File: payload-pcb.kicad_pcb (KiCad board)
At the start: 4 copper layers, 127 x 76.2 mm, 112 parts, among them J1 POWER_IN, J10 GPIO0, J12 I2C, J13 GPIO1, J14 CAN, J15 CAN, J16 SCOOP1, J17 SCOOP2, J18 ACTUATOR, J19 DRILL, J2 POWER_OUT, J20 SERVO5, J21 SERVO6, J22 SERVO7, J23 SERVO8, J5 MOIST, J6 TEMP, J7 POT3, J9 RELAYS, Q1 SUD50P10-43L-GE3, Q2 SUD50P10-43L-GE3, Q3 SUD50P10-43L-GE3, Q4 DMG2305UX, Q5 Q_NMOS, Q6 Q_NMOS, Q7 Q_NMOS, Q8 Q_NMOS, U12 +3V3@2A, U14 Pico, U15 74HCT244, U22 MCP2562, U23 MCP2515, U8 PCA9555PWR, U9 +5V@2A, Y1 8MHz

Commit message: more cleanup and added notes for review
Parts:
- added R20: 1k, Resistor_SMD:R_0805_2012Metric_Pad1.20x1.40mm_HandSolder, F.Cu at (1.88, 0.97)
- added R21: 150, Resistor_SMD:R_0805_2012Metric_Pad1.20x1.40mm_HandSolder, F.Cu at (1.88, 3.92)
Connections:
- net GP21 renamed DIGITAL_GP21
- net GP22 renamed DIGITAL_GP22
- net INT renamed ~{CAN_INTERRUPT}
- net NEW_GP14 renamed DIGITAL_GP14
- net NEW_GP15 renamed DIGITAL_GP15
- J10 pad 1: Net-(J10-Pin_1) -> /GPIO/Payload_S1
- J10 pad 2: Net-(J10-Pin_2) -> /GPIO/Payload_S2
- J10 pad 3: Net-(J10-Pin_3) -> /GPIO/Payload_S3
- J10 pad 4: Net-(J10-Pin_4) -> /GPIO/Payload_S4
- J10 pad 5: /GPIO/Payload_S1 -> Net-(J10-Pin_5)
- J10 pad 6: /GPIO/Payload_S2 -> Net-(J10-Pin_6)
- J10 pad 7: /GPIO/Payload_S3 -> Net-(J10-Pin_7)
- J10 pad 8: /GPIO/Payload_S4 -> Net-(J10-Pin_8)
- U8 pad 10: /GPIO/Payload_S3 -> Net-(J10-Pin_7)
- U8 pad 11: /GPIO/Payload_S4 -> Net-(J10-Pin_8)
- U8 pad 4: Net-(J10-Pin_1) -> /GPIO/Payload_S1
- U8 pad 5: Net-(J10-Pin_2) -> /GPIO/Payload_S2
- U8 pad 6: Net-(J10-Pin_3) -> /GPIO/Payload_S3
- U8 pad 7: Net-(J10-Pin_4) -> /GPIO/Payload_S4
- U8 pad 8: /GPIO/Payload_S1 -> Net-(J10-Pin_5)
- U8 pad 9: /GPIO/Payload_S2 -> Net-(J10-Pin_6)
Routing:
- net (no net): vias 0 -> 102

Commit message: pcb review session notes
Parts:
- removed R20: 1k, Resistor_SMD:R_0805_2012Metric_Pad1.20x1.40mm_HandSolder
- removed R21: 150, Resistor_SMD:R_0805_2012Metric_Pad1.20x1.40mm_HandSolder
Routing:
- net Net-(J10-Pin_8): track 0.00 -> 8.38 mm
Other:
- board text added: "University Rover Challenge Payload PCB v5.0 by Austin Driggs 2025-2026"
- board text removed: "University Rover Challenge Payload PCB by Austin Driggs 2025-2026"

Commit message: major rework again after the meeting
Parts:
- removed C10: 22 uF, Payload_PCB_v3.1:UCM1H220MCL1GS
- removed C11, C12, C13: 0.1 uF, Capacitor_SMD:C_1206_3216Metric_Pad1.33x1.80mm_HandSolder
- removed D11: LED4, LED_SMD:LED_0805_2012Metric_Pad1.15x1.40mm_HandSolder
- removed D12: LED3, LED_SMD:LED_0805_2012Metric_Pad1.15x1.40mm_HandSolder
- removed D4: +40V, LED_SMD:LED_0805_2012Metric_Pad1.15x1.40mm_HandSolder
- removed D6: VDC, LED_SMD:LED_0805_2012Metric_Pad1.15x1.40mm_HandSolder
- removed D7: +5V, LED_SMD:LED_0805_2012Metric_Pad1.15x1.40mm_HandSolder
- removed D8: +3V3, LED_SMD:LED_0805_2012Metric_Pad1.15x1.40mm_HandSolder
- removed F2, F3: Fuse, Fuse:Fuseholder_Blade_Mini_Keystone_3568
- removed J10: GPIO0, Connector_Molex:Molex_PicoBlade_53047-0810_1x08_P1.25mm_Vertical
- removed J13: GPIO1, Connector_Molex:Molex_PicoBlade_53047-0810_1x08_P1.25mm_Vertical
- removed J20: SERVO5, Connector_Molex:Molex_PicoBlade_53047-0310_1x03_P1.25mm_Vertical
- removed J21: SERVO6, Connector_Molex:Molex_PicoBlade_53047-0310_1x03_P1.25mm_Vertical
- removed J22: SERVO7, Connector_Molex:Molex_PicoBlade_53047-0310_1x03_P1.25mm_Vertical
- removed J23: SERVO8, Connector_Molex:Molex_PicoBlade_53047-0310_1x03_P1.25mm_Vertical
- removed JP1, JP2, JP3, JP4: SolderJumper_2_Open, Jumper:SolderJumper-2_P1.3mm_Open_RoundedPad1.0x1.5mm
- removed Q3: SUD50P10-43L-GE3, Package_TO_SOT_SMD:TO-252-2
- removed Q7, Q8: Q_NMOS, Package_TO_SOT_SMD:TSOT-23
- removed R15: 1k, Resistor_SMD:R_0805_2012Metric_Pad1.20x1.40mm_HandSolder
- removed R16, R18: 150, Resistor_SMD:R_0805_2012Metric_Pad1.20x1.40mm_HandSolder
- removed R19: 62, Resistor_SMD:R_0805_2012Metric_Pad1.20x1.40mm_HandSolder
- removed TP14: LED4, TestPoint:TestPoint_Pad_D1.0mm
- removed TP16: LED3, TestPoint:TestPoint_Pad_D1.0mm
- removed TP2: +BATT_IN, TestPoint:TestPoint_Pad_D2.0mm
- removed TP3: +VDC_IN, TestPoint:TestPoint_Pad_D2.0mm
- removed TP4, TP6: +12V_IN, TestPoint:TestPoint_Pad_D2.0mm
- removed U15: 74HCT244, Package_SO:SO-20_12.8x7.5mm_P1.27mm
- removed U8: PCA9555PWR, Package_SO:TSSOP-24_4.4x7.8mm_P0.65mm
- added C8: 0.1 uF, Capacitor_SMD:C_1206_3216Metric_Pad1.33x1.80mm_HandSolder, F.Cu at (162.1, 69.3)
- added J3: UART, Connector_Molex:Molex_PicoBlade_53047-0410_1x04_P1.25mm_Vertical, F.Cu at (191.1, 68.1)
- added J4: USB, Connector_USB:USB_Micro-B_Wuerth_629105150521, F.Cu at (153.2, 69.2)
- added R10: 45m, Resistor_SMD:R_1206_3216Metric_Pad1.30x1.75mm_HandSolder, F.Cu at (121.8, 90.0)
- added R9: 45m, Resistor_SMD:R_1206_3216Metric_Pad1.30x1.75mm_HandSolder, F.Cu at (124.1, 90.0)
- added U1: SN74AHCT126DR, Package_SO:SOIC-14_3.9x8.7mm_P1.27mm, F.Cu at (139.6, 76.1)
- added U2: FT230XS, Package_SO:SSOP-20_3.9x8.7mm_P0.635mm, F.Cu at (166.8, 72.1)
- added U3: LTC2990, Package_SO:MSOP-10_3x3mm_P0.5mm, F.Cu at (132.1, 89.6)
- C1: value 0.1 uF -> 22 uF; footprint Capacitor_SMD:C_1206_3216Metric_Pad1.33x1.80mm_HandSolder -> Capacitor_THT:CP_Radial_D10.0mm_P5.00mm
- C20: footprint Payload_PCB_v3.1:UCM1H220MCL1GS -> Capacitor_SMD:C_Elec_4x5.4
- C4: value 0.1 uF -> 47p; footprint Capacitor_SMD:C_1206_3216Metric_Pad1.33x1.80mm_HandSolder -> Capacitor_SMD:C_0603_1608Metric_Pad1.08x0.95mm_HandSolder
- C5: value 22 uF -> 47p; footprint Payload_PCB_v3.1:UCM1H220MCL1GS -> Capacitor_SMD:C_0603_1608Metric_Pad1.08x0.95mm_HandSolder
- C9: value 0.1 uF -> 470p; footprint Capacitor_SMD:C_1206_3216Metric_Pad1.33x1.80mm_HandSolder -> Capacitor_SMD:C_0603_1608Metric_Pad1.08x0.95mm_HandSolder
- D10: value LED2 -> BAD
- D2, D3: value BZT52C10-TP -> +12V; footprint Diode_SMD:D_SOD-123 -> LED_SMD:LED_0805_2012Metric_Pad1.15x1.40mm_HandSolder
- D9: value LED1 -> GOOD
- F1: footprint Fuse:Fuseholder_Blade_Mini_Keystone_3568 -> Fuse:Fuse_1210_3225Metric
- J1: footprint Connector_Molex:Molex_Mini-Fit_Jr_5569-06A2_2x03_P4.20mm_Horizontal -> Connector_Molex:Molex_Micro-Fit_3.0_43045-0200_2x01_P3.00mm_Horizontal
- J16: value SCOOP1 -> SCOOP
- J17: value SCOOP2 -> MANIPULATOR
- J18: value ACTUATOR -> SERVO3
- J19: value DRILL -> SERVO4
- J2: footprint Connector_Molex:Molex_Mini-Fit_Jr_5569-12A2_2x06_P4.20mm_Horizontal -> Connector_Molex:Molex_Micro-Fit_3.0_43045-0600_2x03_P3.00mm_Horizontal
- J7: value POT3 -> MANIPULATOR
- J9: value RELAYS -> GPIO
- Q2: value SUD50P10-43L-GE3 -> MMBT3904; footprint Package_TO_SOT_SMD:TO-252-2 -> Package_TO_SOT_SMD:SOT-23
- R17: footprint Resistor_SMD:R_0805_2012Metric_Pad1.20x1.40mm_HandSolder -> Resistor_SMD:R_0603_1608Metric_Pad0.98x0.95mm_HandSolder
- R3, R4: value 100k -> 511; footprint Resistor_SMD:R_0805_2012Metric_Pad1.20x1.40mm_HandSolder -> Resistor_SMD:R_0603_1608Metric_Pad0.98x0.95mm_HandSolder
- R6: value 511 -> 27; footprint Resistor_SMD:R_0805_2012Metric_Pad1.20x1.40mm_HandSolder -> Resistor_SMD:R_0603_1608Metric_Pad0.98x0.95mm_HandSolder
- R7: value 10k -> 27; footprint Resistor_SMD:R_0805_2012Metric_Pad1.20x1.40mm_HandSolder -> Resistor_SMD:R_0603_1608Metric_Pad0.98x0.95mm_HandSolder
- R8: value 511 -> 45m; footprint Resistor_SMD:R_0805_2012Metric_Pad1.20x1.40mm_HandSolder -> Resistor_SMD:R_1206_3216Metric_Pad1.30x1.75mm_HandSolder
- TP11: moved to B.Cu
- U14: value Pico -> PI_PICO
- moved C3 57.8 mm to (171.4, 72.6), turned to -90 degrees
- moved G*** 56.5 mm to (175.4, 89.4)
- moved TP10 53.9 mm to (111.8, 123.3), turned to 90 degrees
- moved R4 51.4 mm to (103.8, 102.1), turned to -90 degrees
- moved C1 48.6 mm to (120.9, 74.2), turned to 0 degrees
- moved R3 45.6 mm to (105.4, 102.1), turned to -90 degrees
- moved C4 43.8 mm to (154.9, 73.3), turned to 180 degrees
- moved C5 39.5 mm to (151.6, 73.3)
- moved TP9 39.4 mm to (126.7, 82.5), turned to -90 degrees
- moved R7 38.7 mm to (152.5, 75.7), turned to -90 degrees
- moved D3 37.8 mm to (115.2, 105.5), turned to 180 degrees
- moved R8 35.5 mm to (126.4, 90.0), turned to 90 degrees
- moved D2 34.3 mm to (115.2, 103.4), turned to 180 degrees
- moved C9 33.9 mm to (132.1, 93.6), turned to 180 degrees
- moved J15 33.6 mm to (165.6, 111.6), turned to 180 degrees
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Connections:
- net ANALOG_POT3 renamed ANALOG_MANIPULATOR
- net DIGITAL_GP14 renamed DIGITAL_LIMIT_SW1
- net DIGITAL_GP15 renamed DIGITAL_LIMIT_SW2
- net DIGITAL_GP21 renamed DIGITAL_RELAY1
- net DIGITAL_GP22 renamed DIGITAL_RELAY2
- net LED1 renamed /Pi Pico/LED_GOOD
- net LED2 renamed /Pi Pico/LED_BAD
- C1 pad 1: GND -> +12V
- C1 pad 2: +12V -> GND
- C2 pad 2: +3.3V -> +5V
- C25 pad 1: VDC -> +5V
- C3 pad 2: +BATT -> +5V
- C4 pad 2: +12V -> /USB/USB-
- C5 pad 1: +12V -> GND
- C5 pad 2: GND -> /USB/USB+
- C9 pad 1: GND -> Net-(Q2-E)
- C9 pad 2: +BATT -> Net-(Q2-B)
- D1 pad 1: +12V -> /Power/+12V_PROTECTED
- D10 pad 1: GND -> Net-(D10-K)
- D2 pad 1: +BATT -> GND
- D3 pad 1: Net-(D3-K) -> GND
- D9 pad 1: GND -> Net-(D9-K)
- J1 pad 2: GND -> /Power/+12V_IN
- J12 pad 2: I2C0_SCL -> I2C0_SDA
- J12 pad 3: I2C0_SDA -> I2C0_SCL
- J16 pad 1: VDC -> +5V
- J17 pad 1: VDC -> +5V
- J18 pad 1: VDC -> +5V
- J19 pad 1: VDC -> +5V
- J2 pad 4: GND -> +12V
- J2 pad 5: GND -> +5V
- J2 pad 6: GND -> +3.3V
- Q1 pad 3: +12V -> /Power/+12V_PROTECTED
- Q2 pad 1: Net-(D2-A) -> Net-(Q2-B)
- Q2 pad 2: Net-(Q2-D) -> Net-(Q2-E)
- Q2 pad 3: +BATT -> Net-(Q2-B)
- Q4 pad 3: +3.3V -> +5V
- Q5 pad 1: Net-(Q5-D) -> Net-(D9-K)
- Q5 pad 3: Net-(D9-A) -> GND
- Q6 pad 1: Net-(Q6-D) -> Net-(D10-K)
- Q6 pad 3: Net-(D10-A) -> GND
- R1 pad 1: Net-(Q5-D) -> Net-(D9-A)
- R3 pad 2: GND -> +5V
- R4 pad 2: GND -> +3.3V
- R5 pad 1: Net-(Q6-D) -> Net-(D10-A)
- R6 pad 1: Net-(Q7-D) -> /USB/USB-
- R6 pad 2: +3.3V -> Net-(U2-USBDM)
- R7 pad 1: Net-(U8-~{INT}) -> /USB/USB+
- R7 pad 2: +3.3V -> Net-(U2-USBDP)
- R8 pad 1: Net-(Q8-D) -> /Power/+12V_PROTECTED
- R8 pad 2: +3.3V -> +12V
- U14 pad 10: SERVO6_PICO -> unconnected-(U14-GPIO7-Pad10)
- U14 pad 11: SERVO7_PICO -> /Pi Pico/UART1_TX
- U14 pad 12: SERVO8_PICO -> /Pi Pico/UART1_RX
- U14 pad 16: LED3 -> UART0_TX
- U14 pad 17: LED4 -> UART0_RX
- U14 pad 9: SERVO5_PICO -> unconnected-(U14-GPIO6-Pad9)
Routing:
- net Net-(J10-Pin_8): track 8.38 -> 0.00 mm
- net (no net): vias 102 -> 0
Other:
- board size 127 x 76.2 mm -> 101.6 x 63.5 mm

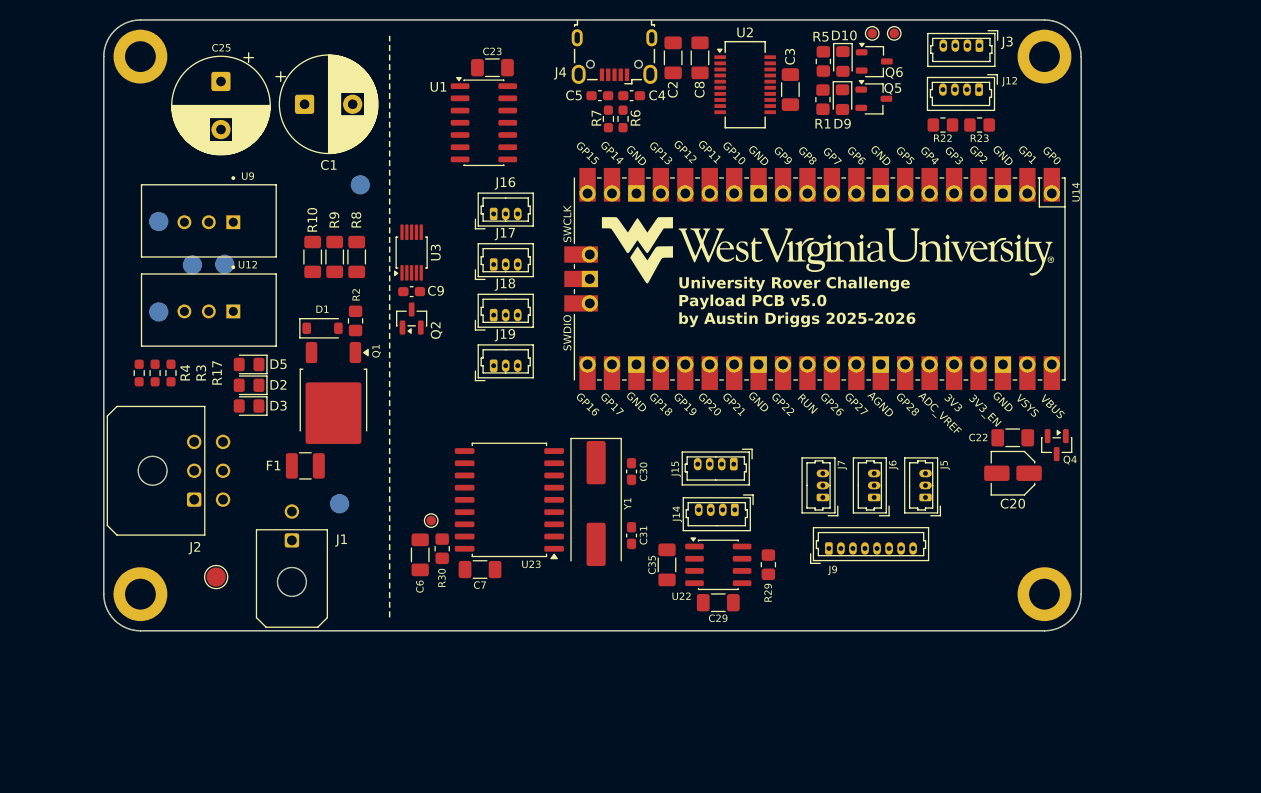
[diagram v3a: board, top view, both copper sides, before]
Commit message: major finishing touches:     - major rework for v5.1     - silkscreen and stuff     - impednace for USB and CAN lines     - schematic comments     - symbol, footprint, and model library updates
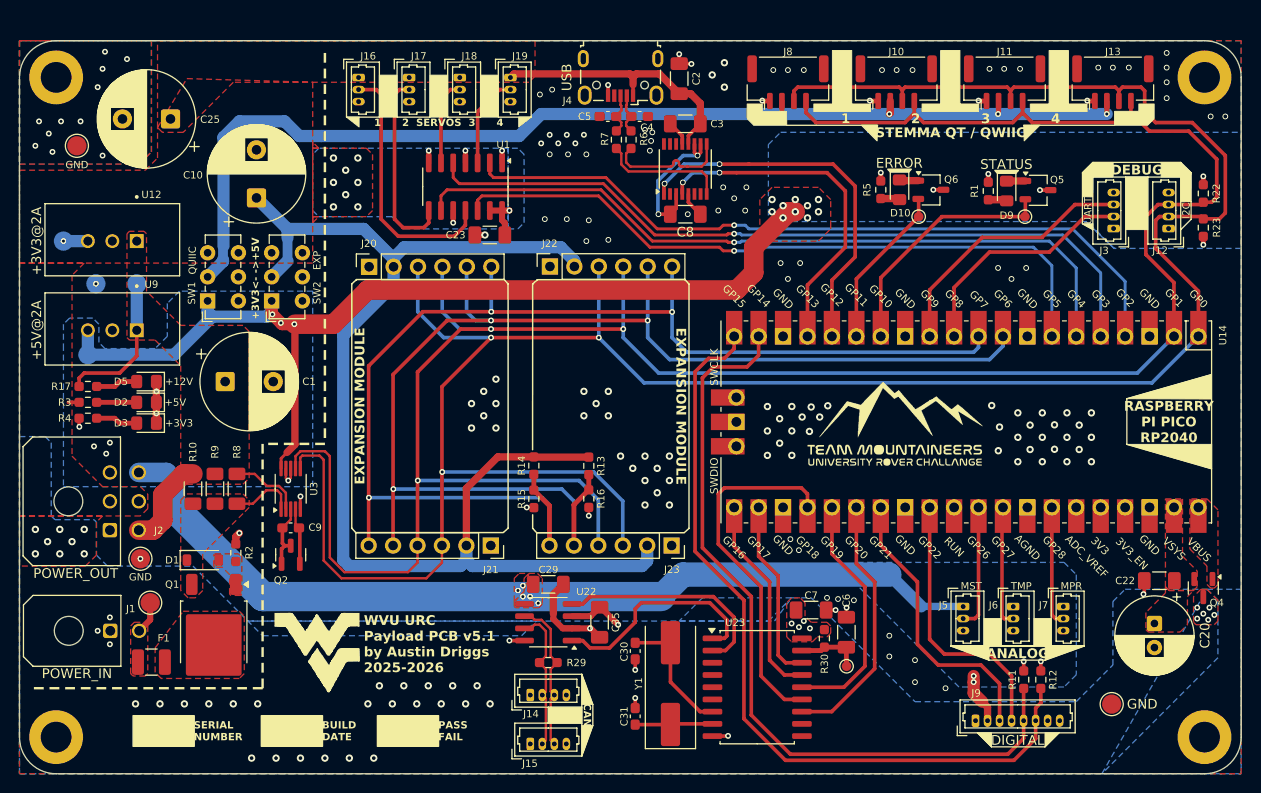
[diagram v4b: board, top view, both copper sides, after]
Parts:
- removed G***: LOGO, Payload_PCB_v3.1:Flying_WV_Logo_Large
- added C10: 1000uF, Capacitor_THT:CP_Radial_D10.0mm_P5.00mm, F.Cu at (116.0, 83.9)
- added J10: QWIIC3, Connector_JST:JST_GH_BM04B-GHS-TBT_1x04-1MP_P1.25mm_Vertical, F.Cu at (182.5, 71.9)
- added J11: QWIIC2, Connector_JST:JST_GH_BM04B-GHS-TBT_1x04-1MP_P1.25mm_Vertical, F.Cu at (193.7, 71.9)
- added J13: QWIIC1, Connector_JST:JST_GH_BM04B-GHS-TBT_1x04-1MP_P1.25mm_Vertical, F.Cu at (205.0, 71.9)
- added J20: EXP1, Connector_PinSocket_2.54mm:PinSocket_1x06_P2.54mm_Vertical, F.Cu at (127.7, 91.1)
- added J21: EXP2, Connector_PinSocket_2.54mm:PinSocket_1x06_P2.54mm_Vertical, F.Cu at (140.3, 120.0)
- added J22: EXP3, Connector_PinSocket_2.54mm:PinSocket_1x06_P2.54mm_Vertical, F.Cu at (146.5, 91.0)
- added J23: EXP4, Connector_PinSocket_2.54mm:PinSocket_1x06_P2.54mm_Vertical, F.Cu at (159.1, 120.0)
- added J8: QWIIC4, Connector_JST:JST_GH_BM04B-GHS-TBT_1x04-1MP_P1.25mm_Vertical, F.Cu at (171.2, 71.9)
- added R11: 10k, Resistor_SMD:R_0603_1608Metric_Pad0.98x0.95mm_HandSolder, F.Cu at (195.7, 134.0)
- added R12: 10k, Resistor_SMD:R_0603_1608Metric_Pad0.98x0.95mm_HandSolder, F.Cu at (197.5, 134.0)
- added R13: 10k, Resistor_SMD:R_0603_1608Metric_Pad0.98x0.95mm_HandSolder, F.Cu at (150.5, 111.8)
- added R14: 10k, Resistor_SMD:R_0603_1608Metric_Pad0.98x0.95mm_HandSolder, F.Cu at (144.8, 111.7)
- added R15: 10k, Resistor_SMD:R_0603_1608Metric_Pad0.98x0.95mm_HandSolder, F.Cu at (144.8, 115.2)
- added R16: 10k, Resistor_SMD:R_0603_1608Metric_Pad0.98x0.95mm_HandSolder, F.Cu at (150.5, 115.2)
- added SW1: QUIIC, Button_Switch_THT:SW_E-Switch_EG1271_SPDT, F.Cu at (110.9, 94.6)
- added SW2: EXP, Button_Switch_THT:SW_E-Switch_EG1271_SPDT, F.Cu at (117.5, 94.6)
- added TP2: GND, TestPoint:TestPoint_Pad_D2.0mm, F.Cu at (204.9, 136.5)
- C1: value 22 uF -> 1000uF
- C2, C22, C23, C29, C3, C35, C6, C7, C8: value 0.1 uF -> 0.1uF
- C20: value 10 uF -> 10uF; footprint Capacitor_SMD:C_Elec_4x5.4 -> Capacitor_THT:CP_Radial_D8.0mm_P2.50mm
- C25: value 100 uF -> 1000uF
- C30, C31: value 22 pF -> 22pF
- D10: value BAD -> ERROR
- D2: value +12V -> +5V
- D3: value +12V -> +3V3
- D9: value GOOD -> STATUS
- F1: value Fuse -> PTC
- J5: value MOIST -> MST
- J6: value TEMP -> TMP
- J7: value MANIPULATOR -> MPR
- J9: value GPIO -> DIGITAL
- Q5, Q6: value Q_NMOS -> 2N7002
- R1, R2, R22, R23, R29, R30, R5: footprint Resistor_SMD:R_0805_2012Metric_Pad1.20x1.40mm_HandSolder -> Resistor_SMD:R_0603_1608Metric_Pad0.98x0.95mm_HandSolder
- R10, R8, R9: value 45m -> 30m
- R6, R7: value 27 -> 22
- TP1: moved to F.Cu
- TP10, TP11: value +12V_IN -> GND
- TP5: value +12V_IN -> +12V
- TP7: value +12V_IN -> +5V
- TP8: value +12V_IN -> +3V3
- TP9: value +12V_IN -> GND; moved to F.Cu
- U12, U9: footprint Payload_PCB_v3.1:CONV_TSR_2-2433 -> footprints:TSR_2-24xx
- U14: footprint MCU_RaspberryPi_and_Boards:RPi_Pico_SMD_TH -> footprints:RPi_Pico_SMD_TH
- U2: footprint Package_SO:SSOP-20_3.9x8.7mm_P0.635mm -> Package_SO:SSOP-16_3.9x4.9mm_P0.635mm
- moved TP15 45.8 mm to (177.3, 132.6), turned to 0 degrees
- moved C6 45.0 mm to (177.3, 129.1), turned to 90 degrees
- moved R30 40.8 mm to (175.0, 129.7), turned to 90 degrees
- moved J15 36.0 mm to (144.4, 140.7), turned to 0 degrees
- moved C7 34.7 mm to (173.6, 126.7)
- moved J16 33.1 mm to (126.6, 71.4), turned to -90 degrees
- moved U23 32.3 mm to (168.0, 134.8), turned to 0 degrees
- moved C1 30.0 mm to (112.7, 103.0)
- moved TP9 29.7 mm to (97.3, 78.5)
- moved J14 28.7 mm to (144.4, 135.6), turned to 0 degrees
- moved R22 28.0 mm to (214.4, 83.4), turned to 90 degrees
- moved C9 27.6 mm to (119.5, 118.2)
- moved Q2 27.6 mm to (119.5, 121.0)
- moved U3 27.6 mm to (119.5, 114.1)
- moved J7 27.5 mm to (199.8, 126.4), turned to -90 degrees
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- renumbered J19 to J16, J18 to J17, J17 to J18, J16 to J19
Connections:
- net /CAN/CAN_H renamed /CAN/CAN+
- net /CAN/CAN_L renamed /CAN/CAN-
- net Net-(U2-USBDM) renamed /USB/USB_OUT-
- net Net-(U2-USBDP) renamed /USB/USB_OUT+
- C29 pad 1: +3.3V -> +3V3
- C8 pad 2: +3.3V -> Net-(U2-3V3OUT)
- J12 pad 1: +3.3V -> +3V3
- J2 pad 6: +3.3V -> +3V3
- J3 pad 1: +3.3V -> +3V3
- J5 pad 1: +3.3V -> +3V3
- J6 pad 1: +3.3V -> +3V3
- J7 pad 1: +3.3V -> +3V3
- J9 pad 1: +3.3V -> +5V
- J9 pad 2: +5V -> +3V3
- R1 pad 2: +3.3V -> +3V3
- R22 pad 2: +3.3V -> +3V3
- R23 pad 2: +3.3V -> +3V3
- R4 pad 2: +3.3V -> +3V3
- R5 pad 2: +3.3V -> +3V3
- TP8 pad 1: +3.3V -> +3V3
- U14 pad 10: unconnected-(U14-GPIO7-Pad10) -> DIGITAL_EXP2
- U14 pad 9: unconnected-(U14-GPIO6-Pad9) -> DIGITAL_EXP1
- U2 pad 10: +3.3V -> Net-(U2-3V3OUT)
- U2 pad 11: +3.3V -> Net-(U2-3V3OUT)
- U2 pad 3: +3.3V -> Net-(U2-3V3OUT)
- U22 pad 5: +3.3V -> +3V3
- U3 pad 10: unconnected-(U3-VCC-Pad10) -> +3V3
- U9 pad 3: +3.3V -> +3V3
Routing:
- net I2C0_SDA: track 0.00 -> 258.5 mm, vias 0 -> 3
- net I2C0_SCL: track 0.00 -> 249.5 mm, vias 0 -> 3
- net +3V3: track 0.00 -> 211.3 mm, vias 0 -> 27
- net /GPIO/+EXP: track 0.00 -> 133.1 mm
- net DIGITAL_EXP1: track 0.00 -> 132.9 mm, vias 0 -> 3
- net DIGITAL_EXP2: track 0.00 -> 129.8 mm, vias 0 -> 3
- net /GPIO/+QUIIC: track 0.00 -> 114.7 mm, vias 0 -> 4
- net DIGITAL_LIMIT_SW2: track 0.00 -> 83.0 mm
- net DIGITAL_LIMIT_SW1: track 0.00 -> 81.8 mm
- net SERVO2_PICO: track 0.00 -> 79.6 mm, vias 0 -> 1
- net SERVO3_PICO: track 0.00 -> 78.4 mm, vias 0 -> 1
- net SERVO1_PICO: track 0.00 -> 77.8 mm, vias 0 -> 1
- net SERVO4_PICO: track 0.00 -> 71.6 mm, vias 0 -> 1
- net +5V: track 0.00 -> 46.2 mm, vias 0 -> 32
- net GND: track 0.00 -> 46.1 mm, vias 0 -> 190
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- added copper zone on F.Cu, net +12V
- added copper zone on B.Cu, net +3V3
- added copper zone on F.Cu, net +3V3
- added copper zone on B.Cu, net +5V
- added copper zone on F.Cu, net +5V
- added copper zone on F.Cu, net /Power/+12V_IN
- added copper zone on F.Cu, net /Power/+12V_PROTECTED
- added copper zone on B.Cu, net GND
- added copper zone on F.Cu, net GND
- added copper zone on In1.Cu, net GND
- added copper zone on In2.Cu, net GND
- added copper zone on F.Cu, net Net-(D1-A)
- added copper zone on F.Cu, net Net-(Q1-D)
- added copper zone on F.Cu, net Net-(Q4-G)
- added copper zone on F.Cu, net Net-(Q4-S)
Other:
- board size 101.6 x 63.5 mm -> 127 x 76.2 mm
- board text added: "+3V3<- ->+5V"
- board text added: "1 2 3 4"
- board text added: "1 2 SERVOS 3 4"
- board text added: "ANALOG"
- board text added: "BUILD DATE"
- board text added: "CAN"
- board text added: "DEBUG"
- board text added: "EXPANSION MODULE"
- board text added: "M3 x4"
- board text added: "PASS FAIL"
- board text added: "RASPBERRY PI PICO RP2040"
- board text added: "SERIAL NUMBER"
- board text added: "STEMMA QT / QWIIC"
- board text added: "WVU URC Payload PCB v5.1 by Austin Driggs 2025-2026"
- board text removed: "University Rover Challenge Payload PCB v5.0 by Austin Driggs 2025-2026"
